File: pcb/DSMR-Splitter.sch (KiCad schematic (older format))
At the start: 43 parts, among them J1 IN, J2 OUT-A, J3 OUT-B, J4 OUT-C, J5 JTAG, J6 UART, U1 74AHCT1G04, U2 74AHC1G126, U3 74AHCT1G04, U4 74AHCT1G04, U5 74AHCT1G04, U6 TPS76933, U7 EFM32PG12B500, Y1 40MHz

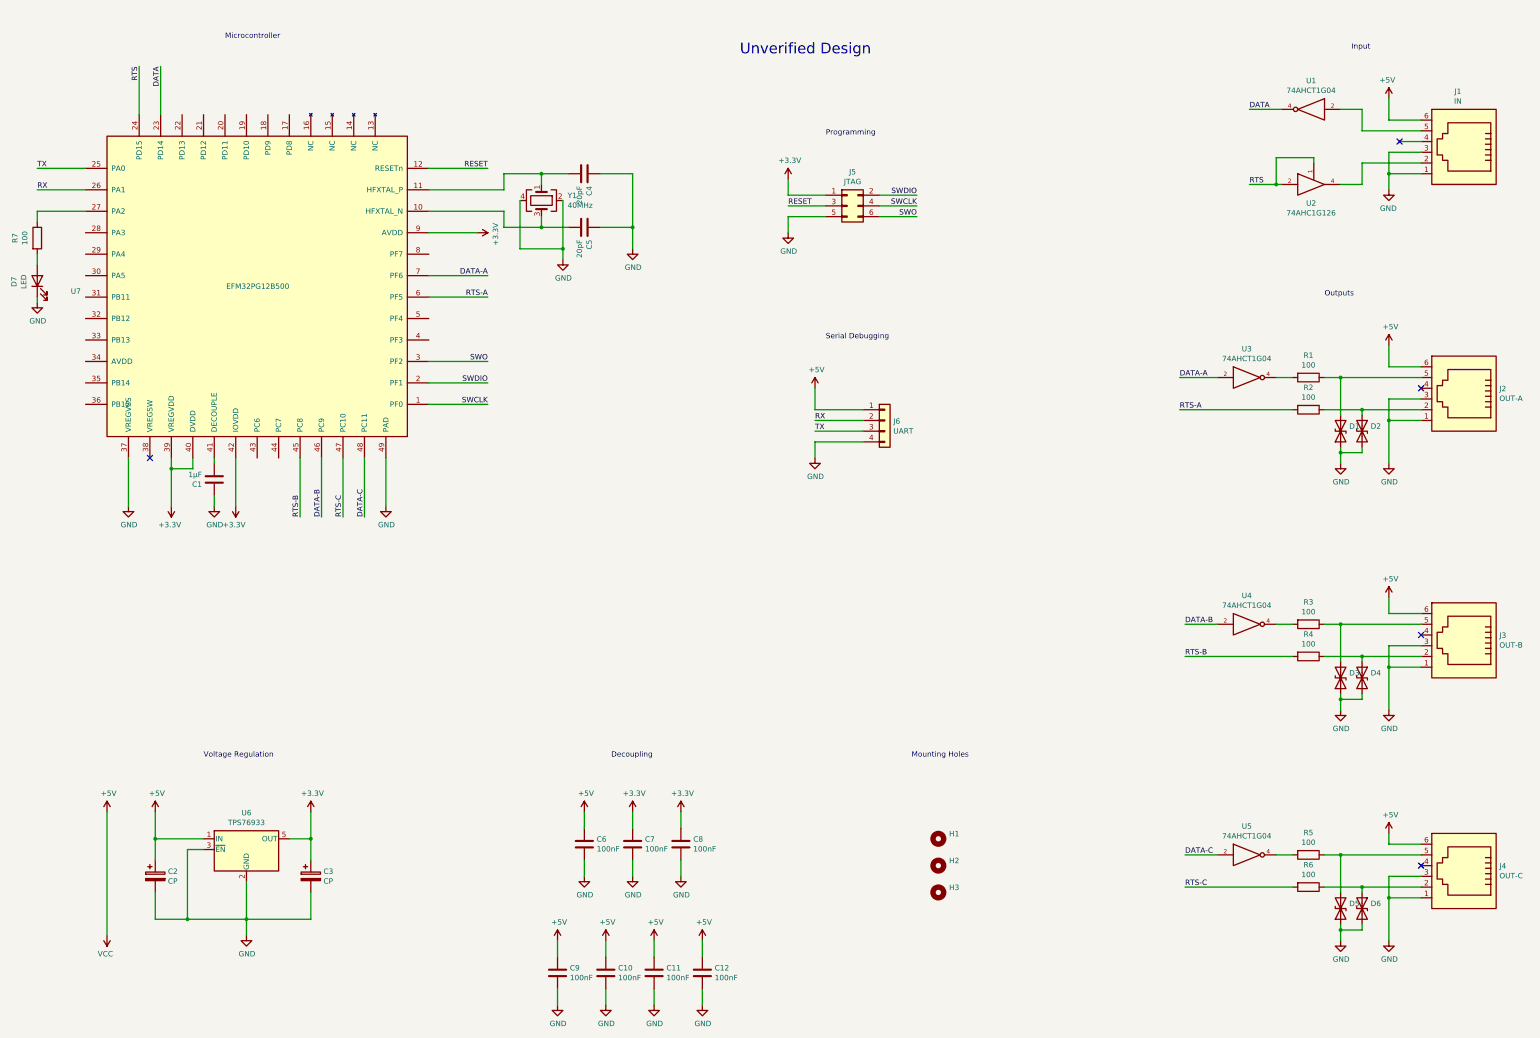
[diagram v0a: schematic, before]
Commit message: Add board version 2.0.0
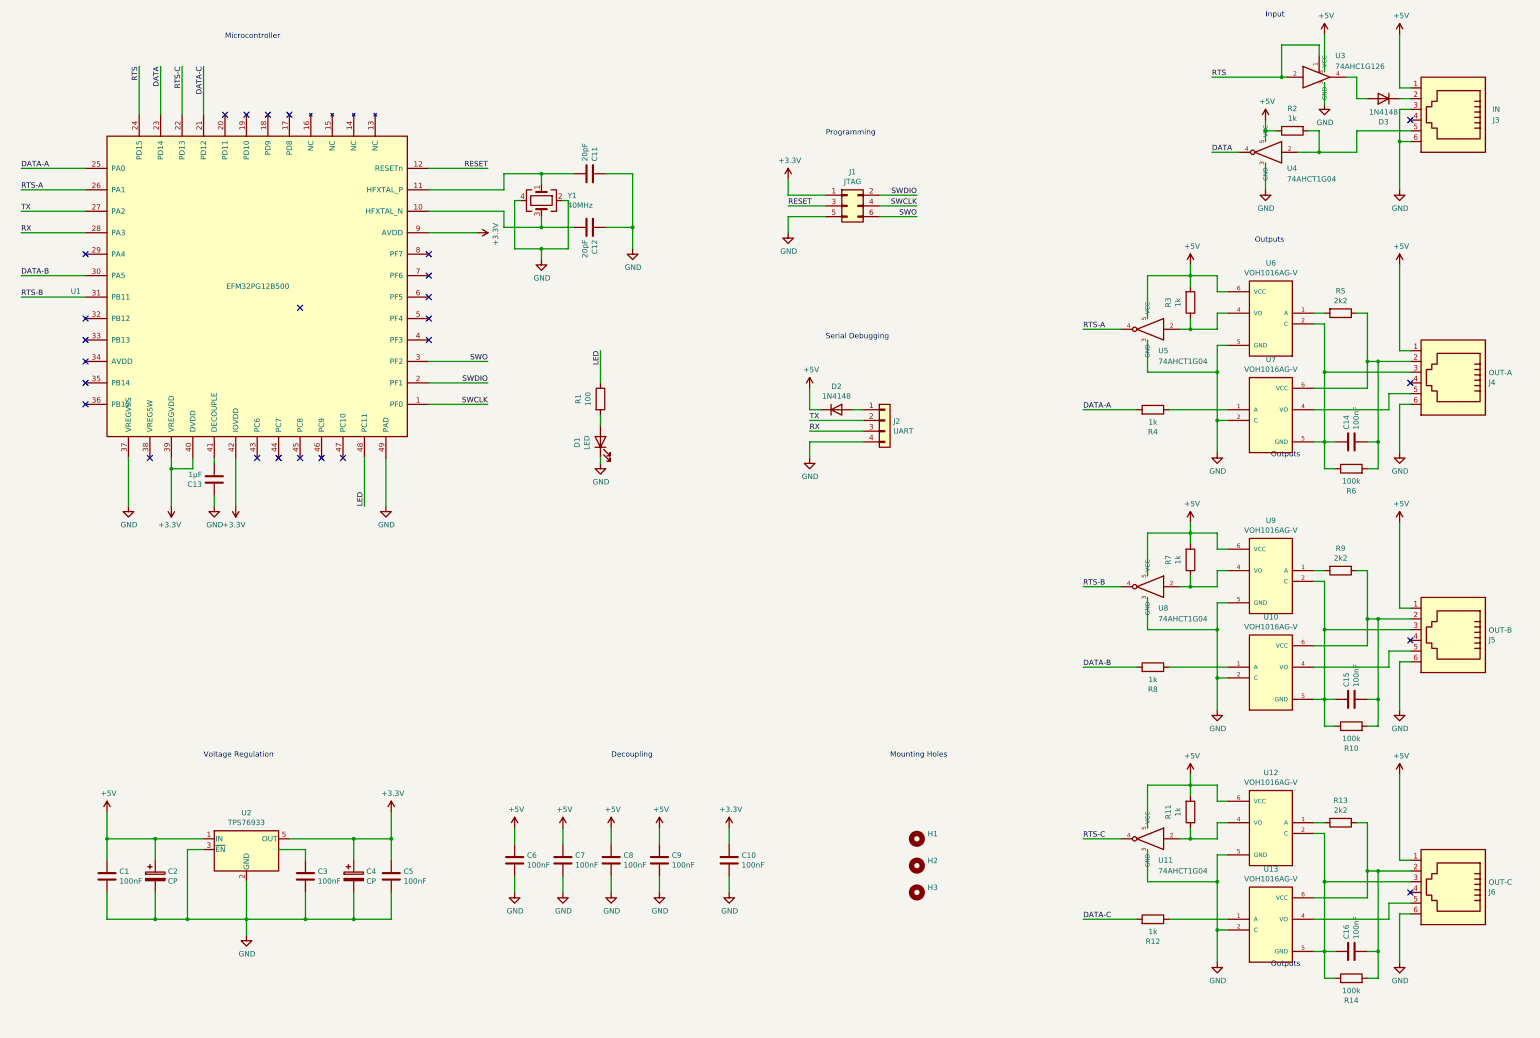
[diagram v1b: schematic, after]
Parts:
- removed C11, C12: 100nF, Capacitor_SMD:C_0603_1608Metric, symbol Device:C
- removed D1, D2, D3, D4, D5, D6: D_TVS, Diode_SMD:D_0603_1608Metric, symbol Device:D_TVS
- removed R1: 100, Resistor_SMD:R_0603_1608Metric, symbol Device:R
- removed U1, U3, U4, U5: 74AHCT1G04, Package_TO_SOT_SMD:SOT-23-5, symbol 74xGxx:74AHCT1G04
- removed U2: 74AHC1G126, Package_TO_SOT_SMD:SOT-23-5, symbol 74xGxx:74AHC1G126
- added C14, C15, C16, C3, C7, C9: 100nF, Capacitor_SMD:C_0603_1608Metric, symbol Device:C
- added D2, D3: 1N4148, Diode_SMD:D_0603_1608Metric, symbol Device:D
- added R10, R14: 100k, Resistor_SMD:R_0603_1608Metric, symbol Device:R
- added R11, R12, R7, R8: 1k, Resistor_SMD:R_0603_1608Metric, symbol Device:R
- added R13, R9: 2k2, Resistor_SMD:R_0603_1608Metric, symbol Device:R
- added U10, U12, U13, U6, U7, U9: VOH1016AG-V, Package_DIP:SMDIP-6_W7.62mm, symbol voh1016:VOH1016AG-V
- added U11, U4, U5, U8: 74AHCT1G04, Package_TO_SOT_SMD:SOT-23-5, symbol 74xx_nohidden:74AHCT1G04
- added U3: 74AHC1G126, Package_TO_SOT_SMD:SOT-23-5, symbol 74xx_nohidden:74AHC1G126
- C2: footprint Capacitor_Tantalum_SMD:CP_EIA-1608-08_AVX-J -> Capacitor_Tantalum_SMD:CP_EIA-3216-12_Kemet-S
- C4: renamed from C3; footprint Capacitor_Tantalum_SMD:CP_EIA-1608-08_AVX-J -> Capacitor_Tantalum_SMD:CP_EIA-3216-12_Kemet-S
- H1, H2, H3: footprint MountingHole:MountingHole_3.2mm_M3 -> MountingHole:MountingHole_2.2mm_M2
- J1: renamed from J5; footprint Connector_PinHeader_2.54mm:PinHeader_2x03_P2.54mm_Vertical -> Connector_PinHeader_1.27mm:PinHeader_2x03_P1.27mm_Vertical
- J2: renamed from J6; footprint Connector_PinHeader_2.54mm:PinHeader_1x04_P2.54mm_Vertical -> Connector_PinHeader_1.27mm:PinHeader_1x04_P1.27mm_Vertical
- R2, R3, R4: value 100 -> 1k
- R5: value 100 -> 2k2
- R6: value 100 -> 100k
- renumbered C6 to C1, C4 to C11, C5 to C12, C1 to C13, C7 to C5, C9 to C6, D7 to D1, J1 to J3, J2 to J4, J3 to J5, J4 to J6, R7 to R1, U7 to U1, U6 to U2
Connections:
- net +3V3: now also C10.1; no longer C8.1
- net +5V: now also C8.1, J3.1, J4.1, J5.1, J6.1, R2.1, R3.2, C7.1, C9.1, D2.1 (K), R11.2, R7.2, U11.5 (VCC), U12.6 (VCC), U3.5 (VCC), U4.5 (VCC), U5.5 (VCC), U6.6 (VCC), U8.5 (VCC), U9.6 (VCC); no longer C10.1, J2.1 (Pin_1), J3.6, J4.6, J5.6, J6.6
- net DATA: now also U4.4
- net DATA-A: now also R4.2, U1.25 (PA0); no longer U1.7 (PF6)
- net DATA-B: now also U1.30 (PA5), R8.2; no longer U1.46 (PC9)
- net DATA-C: now also U1.21 (PD12), R12.2; no longer U1.48 (PC11)
- net GND: now also J3.6, J4.6, J5.6, J6.6, C3.2, C7.2, C9.2, U10.2 (C), U11.3 (GND), U12.5 (GND), U13.2 (C), U3.3 (GND), U4.3 (GND), U5.3 (GND), U6.5 (GND), U7.2 (C), U8.3 (GND), U9.5 (GND); no longer J3.1, J4.1, J4.3, J5.1, J5.3, J6.1, J6.3
- net RTS: now also U3.1, U3.2
- net RTS-A: now also U1.26 (PA1), U5.4; no longer R2.2, U1.6 (PF5)
- net RTS-B: now also U1.31 (PB11), U8.4; no longer R4.2, U1.45 (PC8)
- net RTS-C: now also U1.22 (PD13), U11.4; no longer R6.2, U1.47 (PC10)
- net RX: now also J2.3 (Pin_3), U1.28 (PA3); no longer J2.2 (Pin_2), U1.26 (PA1)
- net TX: now also J2.2 (Pin_2), U1.27 (PA2); no longer J2.3 (Pin_3), U1.25 (PA0)
- net at J3.2: now also D3.1 (K)
- net at J3.5: now also R2.2, U4.2
- net at J4.2: now also R5.1, R6.2, C14.2, U7.6 (VCC); no longer R2.1
- net at J4.5: now also U7.4 (VO)
- net at J5.2: now also C15.2, R10.2, R9.1, U10.6 (VCC); no longer R4.1
- net at J5.5: now also U10.4 (VO); no longer R3.1
- net at R6.1: now also J4.3, C14.1, U6.2 (C), U7.5 (GND); no longer J6.2
- net at J6.5: now also U13.4 (VO); no longer R5.1
- net at R5.2: now also U6.1 (A)
- net at U2.4 (NC): now also C3.1
- net LED: now reaches R1.1
- net LED: now also U1.48 (PC11); no longer U1.27 (PA2)
- new net: C15.1, J5.3, R10.1, U10.5 (GND), U9.2 (C)
- new net: C16.2, J6.2, R13.1, R14.2, U13.6 (VCC)
- new net: C16.1, J6.3, R14.1, U12.2 (C), U13.5 (GND)
- new net: D2.2 (A), J2.1 (Pin_1)
- new net: R3.1, U5.2, U6.4 (VO)
- new net: D3.2 (A), U3.4
- new net: R4.1, U7.1 (A)
- new net: R8.1, U10.1 (A)
- new net: R9.2, U9.1 (A)
- new net: R7.1, U8.2, U9.4 (VO)
- new net: R12.1, U13.1 (A)
- new net: R13.2, U12.1 (A)
- new net: R11.1, U11.2, U12.4 (VO)
- no-connect marks 5 -> 26
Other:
- note removed: "Unverified Design"
- moved on the sheet: C1, C10, C11, C12, C4, C5, C6, D1, H1, H2, H3, J3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
